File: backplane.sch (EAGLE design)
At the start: 11 parts

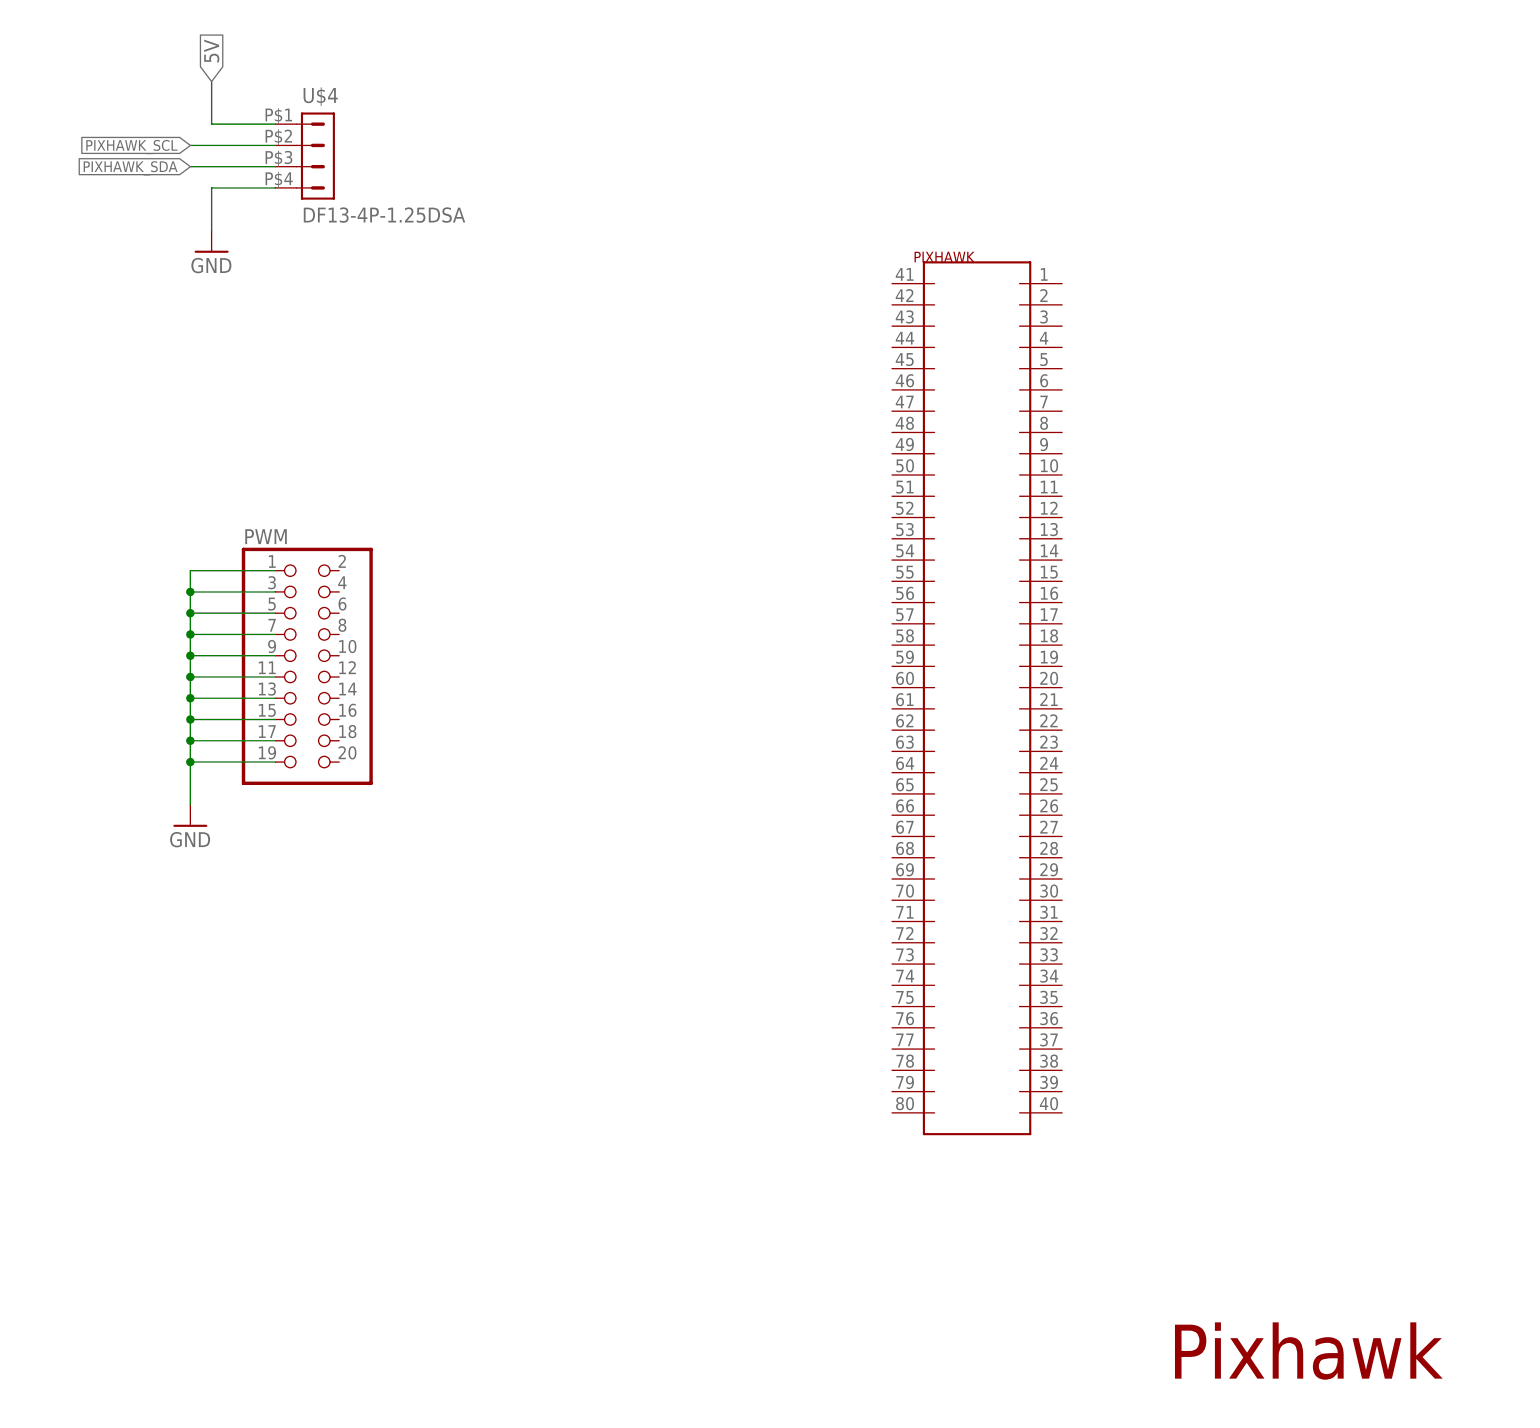
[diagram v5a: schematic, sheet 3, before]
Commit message: Add pixhawk connectors
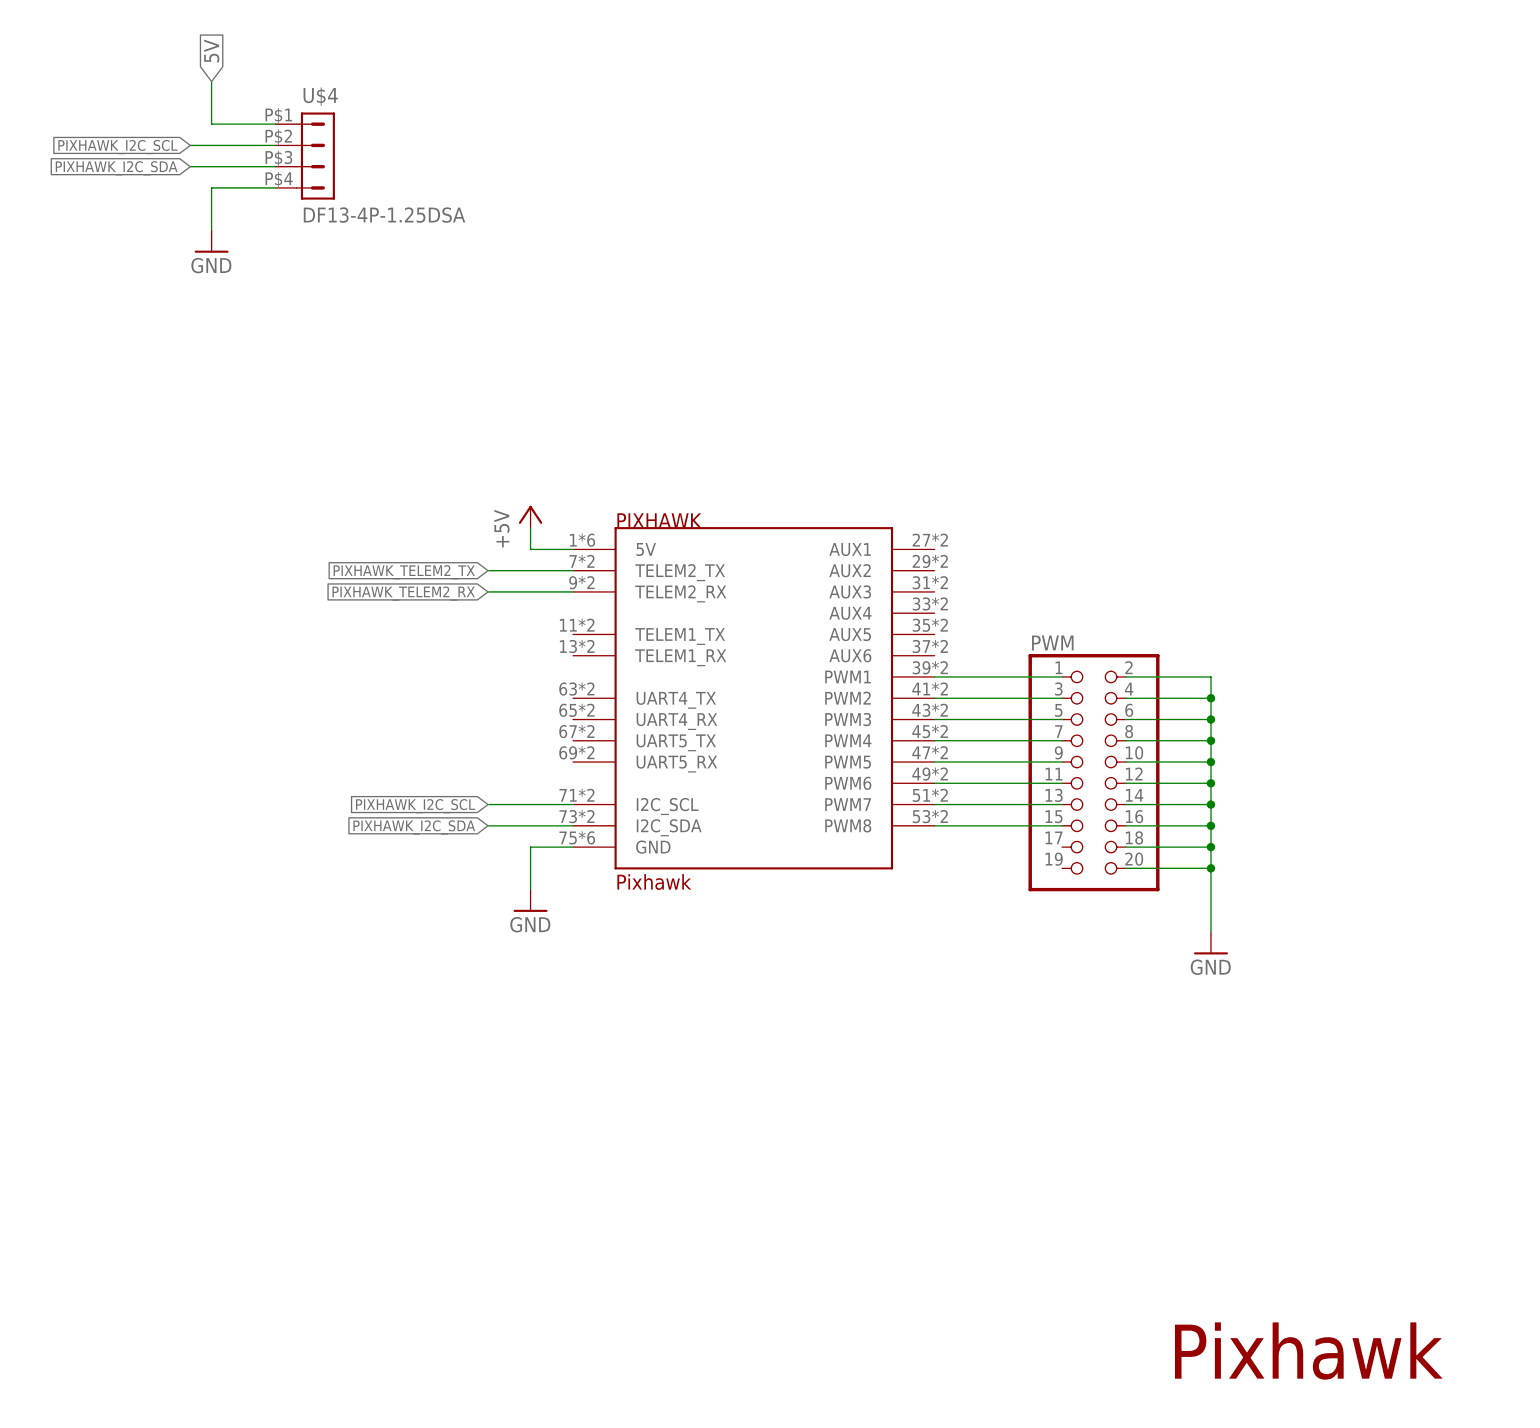
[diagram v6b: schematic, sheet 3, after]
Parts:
- PIXHAWK: value TE-2-5530843-0 -> PIXHAWK_EDGE_CONNCONN; device auv:TE-2-5530843-0 -> auv:PIXHAWK_EDGE_CONNCONN
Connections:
- removed net PIXHAWK_SCL: U$4.2
- removed net PIXHAWK_SDA: U$4.3
- new net N$1: PIXHAWK.PWM1, PWM.1
- new net N$10: PIXHAWK.PWM7, PWM.13
- new net N$11: PIXHAWK.PWM8, PWM.15
- new net N$2: PIXHAWK.PWM2, PWM.3
- new net N$6: PIXHAWK.PWM3, PWM.5
- new net N$7: PIXHAWK.PWM4, PWM.7
- new net N$8: PIXHAWK.PWM5, PWM.9
- new net N$9: PIXHAWK.PWM6, PWM.11
- new net PIXHAWK_I2C_SCL: PIXHAWK.I2C_SCL, U$4.2
- new net PIXHAWK_I2C_SDA: PIXHAWK.I2C_SDA, U$4.3
- net +5V: now also PIXHAWK.5V
- net GND: now also PIXHAWK.GND, PWM.10, PWM.12, PWM.14, PWM.16, PWM.18, PWM.2, PWM.20, PWM.4, PWM.6, PWM.8; no longer PWM.1, PWM.11, PWM.13, PWM.15, PWM.17, PWM.19, PWM.3, PWM.5, PWM.7, PWM.9
- net PIXHAWK_TELEM2_RX: now also PIXHAWK.TELEM2_RX
- net PIXHAWK_TELEM2_TX: now also PIXHAWK.TELEM2_TX
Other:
- moved on the sheet: PWM

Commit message: Add RS232-UART converter
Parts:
- added C1: (no value), auv:C-EUC0603
- added IC1: MAX3233ECWP, auv:MAX3233ECWP
- added MODEM: (no value), auv:PINHD-1X8
- renumbered U$2 to BAT, U$4 to DEPTH
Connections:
- net N$1 renamed PWM1
- net N$10 renamed PWM7
- net N$11 renamed PWM8
- net N$2 renamed PWM2
- net N$6 renamed PWM3
- net N$7 renamed PWM4
- net N$8 renamed PWM5
- net N$9 renamed PWM6
- new net +3V3: C1.1, IC1P.VCC
- new net MODEM_RS232_RX: IC1Q.R1IN
- new net MODEM_RS232_TX: IC1Q.T1OUT
- new net MODEM_RX: IC1Q.R1OUT
- new net MODEM_TX: IC1Q.T1IN
- new net PIXHAWK_GPIO3: PWM.17, U$3.GPIO3
- net GND: now also C1.2, IC1P.GND
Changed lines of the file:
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@@
 <part name="GND7" library="auv" deviceset="GND" device=""/>
 <part name="POWER" library="auv" deviceset="TE-5-5530843-0" device=""/>
-<part name="U$2" library="auv" deviceset="XT-60" device=""/>
+<part name="BAT" library="auv" deviceset="XT-60" device=""/>
 <part name="GND8" library="auv" deviceset="GND" device=""/>
-<part name="U$4" library="auv" deviceset="DF13-4P-1.25" device="DSA"/>
+<part name="DEPTH" library="auv" deviceset="DF13-4P-1.25" device="DSA"/>
 <part name="GND9" library="auv" deviceset="GND" device=""/>
 <part name="PIXHAWK" library="auv" deviceset="PIXHAWK_EDGE_CONN" device="CONN"/>
@@
 <part name="GND10" library="auv" deviceset="GND" device=""/>
 <part name="P+3" library="auv" deviceset="+5V" device=""/>
+<part name="MODEM" library="auv" deviceset="PINHD-1X8" device=""/>
+<part name="IC1" library="auv" deviceset="MAX3233E" device="WP" technology="C"/>
+<part name="+3V1" library="auv" deviceset="+3V3" device=""/>
+<part name="GND11" library="auv" deviceset="GND" device=""/>
+<part name="C1" library="auv" deviceset="C-EU" device="C0603"/>
+<part name="GND12" library="auv" deviceset="GND" device=""/>
 </parts>
 <sheets>
@@
 <instance part="GND3" gate="1" x="83.82" y="109.22"/>
 <instance part="GND4" gate="1" x="83.82" y="96.52"/>
+<instance part="MODEM" gate="A" x="147.32" y="53.34"/>
+<instance part="IC1" gate="Q" x="88.9" y="55.88"/>
+<instance part="+3V1" gate="G$1" x="48.26" y="88.9"/>
+<instance part="IC1" gate="P" x="48.26" y="76.2"/>
+<instance part="GND11" gate="1" x="48.26" y="63.5"/>
+<instance part="C1" gate="G$1" x="58.42" y="81.28"/>
+<instance part="GND12" gate="1" x="58.42" y="71.12"/>
 </instances>
 <busses>
@@
 <wire x1="88.9" y1="111.76" x2="83.82" y2="111.76" width="0.1524" layer="91"/>
 <junction x="88.9" y="111.76"/>
+</segment>
+<segment>
+<pinref part="GND11" gate="1" pin="GND"/>
+<pinref part="IC1" gate="P" pin="GND"/>
+<wire x1="48.26" y1="66.04" x2="48.26" y2="68.58" width="0.1524" layer="91"/>
+</segment>
+<segment>
+<pinref part="C1" gate="G$1" pin="2"/>
+<pinref part="GND12" gate="1" pin="GND"/>
+<wire x1="58.42" y1="76.2" x2="58.42" y2="73.66" width="0.1524" layer="91"/>
 </segment>
 </net>
@@
 <wire x1="175.26" y1="144.78" x2="182.88" y2="144.78" width="0.1524" layer="91"/>
 <label x="182.88" y="144.78" size="1.27" layer="95" xref="yes"/>
+</segment>
+</net>
+<net name="PIXHAWK_GPIO3" class="0">
+<segment>
+<pinref part="U$3" gate="G$1" pin="GPIO3"/>
+<wire x1="175.26" y1="129.54" x2="182.88" y2="129.54" width="0.1524" layer="91"/>
+<label x="182.88" y="129.54" size="1.27" layer="95" xref="yes"/>
+</segment>
+</net>
+<net name="MODEM_RS232_TX" class="0">
+<segment>
+<pinref part="IC1" gate="Q" pin="T1OUT"/>
+<wire x1="101.6" y1="55.88" x2="109.22" y2="55.88" width="0.1524" layer="91"/>
+<label x="109.22" y="55.88" size="1.27" layer="95" xref="yes"/>
+</segment>
+</net>
+<net name="MODEM_RS232_RX" class="0">
+<segment>
+<pinref part="IC1" gate="Q" pin="R1IN"/>
+<wire x1="101.6" y1="48.26" x2="109.22" y2="48.26" width="0.1524" layer="91"/>
+<label x="109.22" y="48.26" size="1.27" layer="95" xref="yes"/>
+</segment>
+</net>
+<net name="MODEM_TX" class="0">
+<segment>
+<pinref part="IC1" gate="Q" pin="T1IN"/>
+<wire x1="76.2" y1="55.88" x2="68.58" y2="55.88" width="0.1524" layer="91"/>
+<label x="68.58" y="55.88" size="1.27" layer="95" rot="R180" xref="yes"/>
+</segment>
+</net>
+<net name="MODEM_RX" class="0">
+<segment>
+<pinref part="IC1" gate="Q" pin="R1OUT"/>
+<wire x1="76.2" y1="48.26" x2="68.58" y2="48.26" width="0.1524" layer="91"/>
+<label x="68.58" y="48.26" size="1.27" layer="95" rot="R180" xref="yes"/>
+</segment>
+</net>
+<net name="+3V3" class="0">
+<segment>
+<pinref part="IC1" gate="P" pin="VCC"/>
+<pinref part="+3V1" gate="G$1" pin="+3V3"/>
+<wire x1="48.26" y1="83.82" x2="48.26" y2="86.36" width="0.1524" layer="91"/>
+<pinref part="C1" gate="G$1" pin="1"/>
+<wire x1="48.26" y1="83.82" x2="58.42" y2="83.82" width="0.1524" layer="91"/>
+<junction x="48.26" y="83.82"/>
 </segment>
 </net>
@@
 <instance part="FRAME2" gate="G$2" x="172.72" y="0"/>
 <instance part="POWER" gate="G$1" x="132.08" y="109.22"/>
-<instance part="U$2" gate="G$1" x="93.98" y="167.64"/>
+<instance part="BAT" gate="G$1" x="93.98" y="167.64"/>
 <instance part="GND8" gate="1" x="83.82" y="157.48"/>
 </instances>
@@
 <net name="VBAT" class="0">
 <segment>
-<pinref part="U$2" gate="G$1" pin="1"/>
+<pinref part="BAT" gate="G$1" pin="1"/>
 <wire x1="88.9" y1="167.64" x2="83.82" y2="167.64" width="0.1524" layer="91"/>
 <wire x1="83.82" y1="167.64" x2="83.82" y2="177.8" width="0.1524" layer="91"/>
@@
 <net name="GND" class="0">
 <segment>
-<pinref part="U$2" gate="G$1" pin="2"/>
+<pinref part="BAT" gate="G$1" pin="2"/>
 <wire x1="88.9" y1="165.1" x2="83.82" y2="165.1" width="0.1524" layer="91"/>
 <wire x1="83.82" y1="165.1" x2="83.82" y2="160.02" width="0.1524" layer="91"/>
@@
 <instance part="FRAME3" gate="G$2" x="172.72" y="0"/>
 <instance part="PWM" gate="A" x="165.1" y="99.06"/>
-<instance part="U$4" gate="G$1" x="73.66" y="172.72"/>
+<instance part="DEPTH" gate="G$1" x="73.66" y="172.72"/>
 <instance part="GND9" gate="1" x="60.96" y="160.02"/>
 <instance part="PIXHAWK" gate="G$1" x="127" y="109.22"/>
@@
 <net name="GND" class="0">
 <segment>
-<pinref part="U$4" gate="G$1" pin="4"/>
+<pinref part="DEPTH" gate="G$1" pin="4"/>
 <wire x1="68.58" y1="167.64" x2="60.96" y2="167.64" width="0.1524" layer="91"/>
 <pinref part="GND9" gate="1" pin="GND"/>
@@
 <net name="5V" class="0">
 <segment>
-<pinref part="U$4" gate="G$1" pin="1"/>
+<pinref part="DEPTH" gate="G$1" pin="1"/>
 <wire x1="68.58" y1="175.26" x2="60.96" y2="175.26" width="0.1524" layer="91"/>
 <wire x1="60.96" y1="175.26" x2="60.96" y2="180.34" width="0.1524" layer="91"/>
@@
 </segment>
 </net>
-<net name="N$1" class="0">
+<net name="PWM1" class="0">
 <segment>
 <pinref part="PIXHAWK" gate="G$1" pin="PWM1"/>
@@
 </segment>
 </net>
-<net name="N$2" class="0">
+<net name="PWM2" class="0">
 <segment>
 <pinref part="PWM" gate="A" pin="3"/>
@@
 </segment>
 </net>
-<net name="N$6" class="0">
+<net name="PWM3" class="0">
 <segment>
 <pinref part="PIXHAWK" gate="G$1" pin="PWM3"/>
@@
 </segment>
 </net>
-<net name="N$7" class="0">
+<net name="PWM4" class="0">
 <segment>
 <pinref part="PWM" gate="A" pin="7"/>
@@
 </segment>
 </net>
-<net name="N$8" class="0">
+<net name="PWM5" class="0">
 <segment>
 <pinref part="PIXHAWK" gate="G$1" pin="PWM5"/>
@@
 </segment>
 </net>
-<net name="N$9" class="0">
+<net name="PWM6" class="0">
 <segment>
 <pinref part="PWM" gate="A" pin="11"/>
@@
 </segment>
 </net>
-<net name="N$10" class="0">
+<net name="PWM7" class="0">
 <segment>
 <pinref part="PIXHAWK" gate="G$1" pin="PWM7"/>
@@
 </segment>
 </net>
-<net name="N$11" class="0">
+<net name="PWM8" class="0">
 <segment>
 <pinref part="PWM" gate="A" pin="15"/>
@@
 </segment>
 <segment>
-<pinref part="U$4" gate="G$1" pin="3"/>
+<pinref part="DEPTH" gate="G$1" pin="3"/>
 <wire x1="68.58" y1="170.18" x2="58.42" y2="170.18" width="0.1524" layer="91"/>
 <label x="58.42" y="170.18" size="1.27" layer="95" rot="R180" xref="yes"/>
@@
 </segment>
 <segment>
-<pinref part="U$4" gate="G$1" pin="2"/>
+<pinref part="DEPTH" gate="G$1" pin="2"/>
 <wire x1="68.58" y1="172.72" x2="58.42" y2="172.72" width="0.1524" layer="91"/>
 <label x="58.42" y="172.72" size="1.27" layer="95" rot="R180" xref="yes"/>
 </segment>
 </net>
+<net name="PIXHAWK_GPIO3" class="0">
+<segment>
+<pinref part="PWM" gate="A" pin="17"/>
+<wire x1="162.56" y1="88.9" x2="147.32" y2="88.9" width="0.1524" layer="91"/>
+<wire x1="147.32" y1="88.9" x2="147.32" y2="78.74" width="0.1524" layer="91"/>
+<label x="147.32" y="78.74" size="1.27" layer="95" rot="R270" xref="yes"/>
+</segment>
+</net>
